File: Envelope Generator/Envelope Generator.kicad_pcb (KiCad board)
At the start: 2 copper layers, 91.3 x 104.5 mm, 71 parts, among them J101 Conn_02x05_Odd_Even, J201 AudioJack2_SwitchT, J301 AudioJack2_SwitchT, J302 AudioJack2_SwitchT, J303 AudioJack2_SwitchT, J304 AudioJack2_SwitchT, Q201 BC547, Q202 BC547, Q203 BC547, SW201 SW_SPST, SW202 SW_SPDT, U101 TL072, U102 TL072, U103 TL072, U104 TL072, U201 ICM7555xP

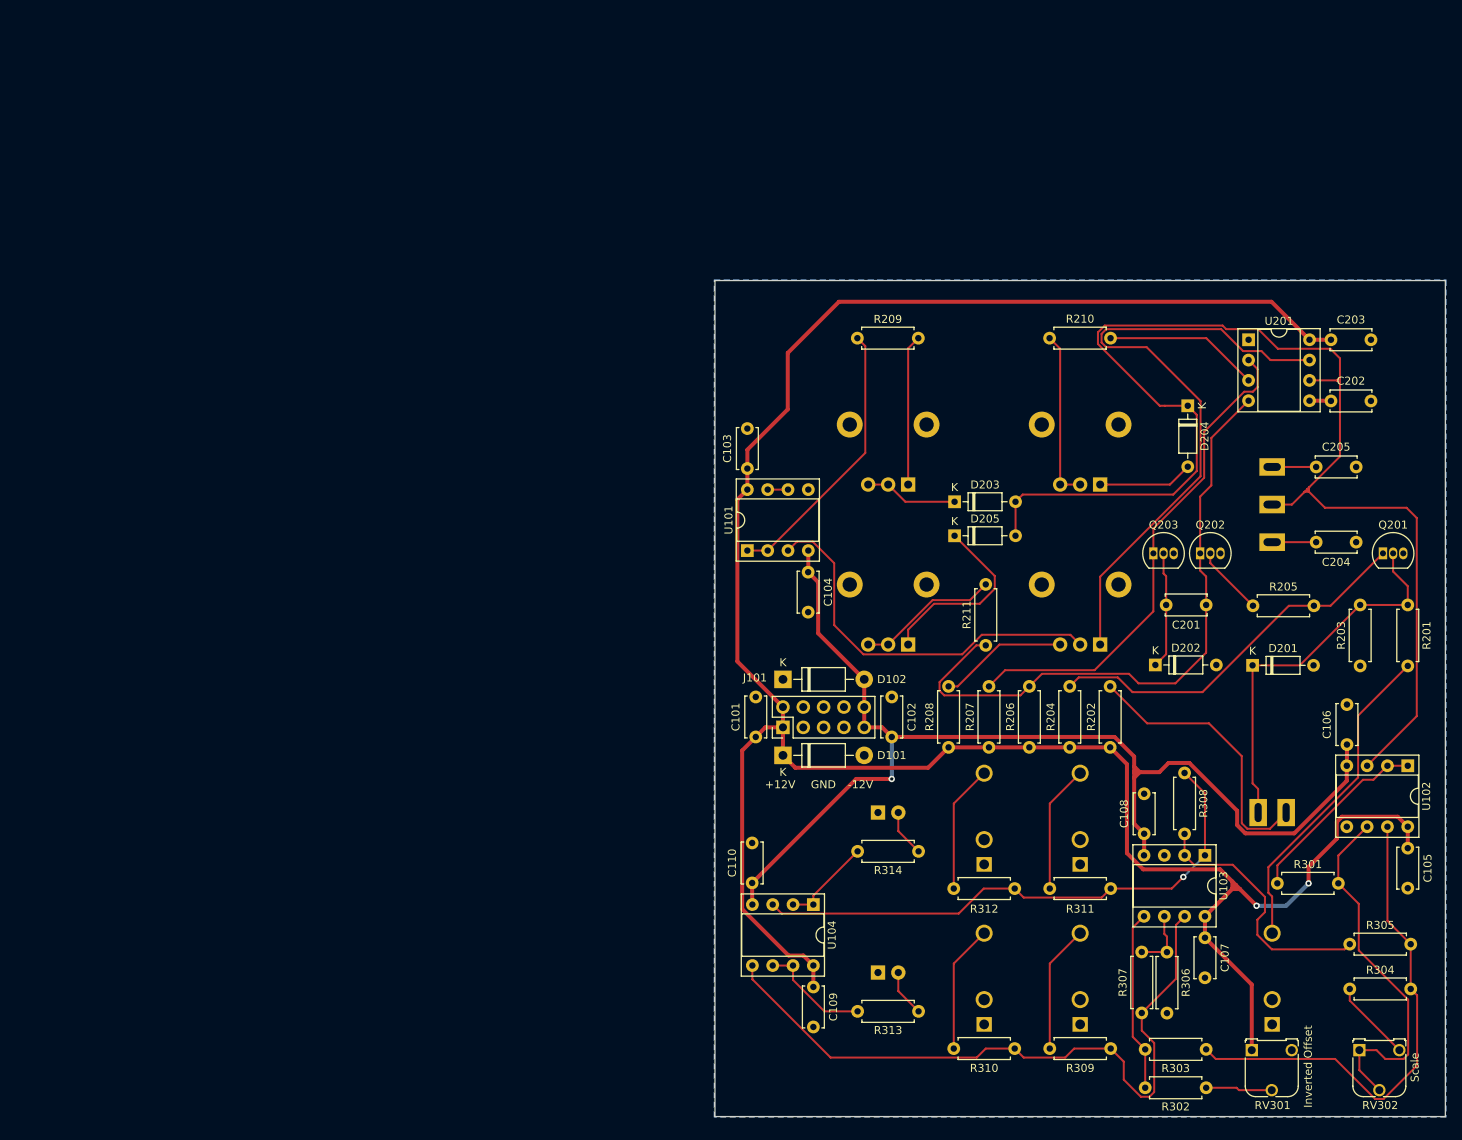
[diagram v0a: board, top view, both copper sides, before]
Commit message: New MIDI controller, new envelope generator
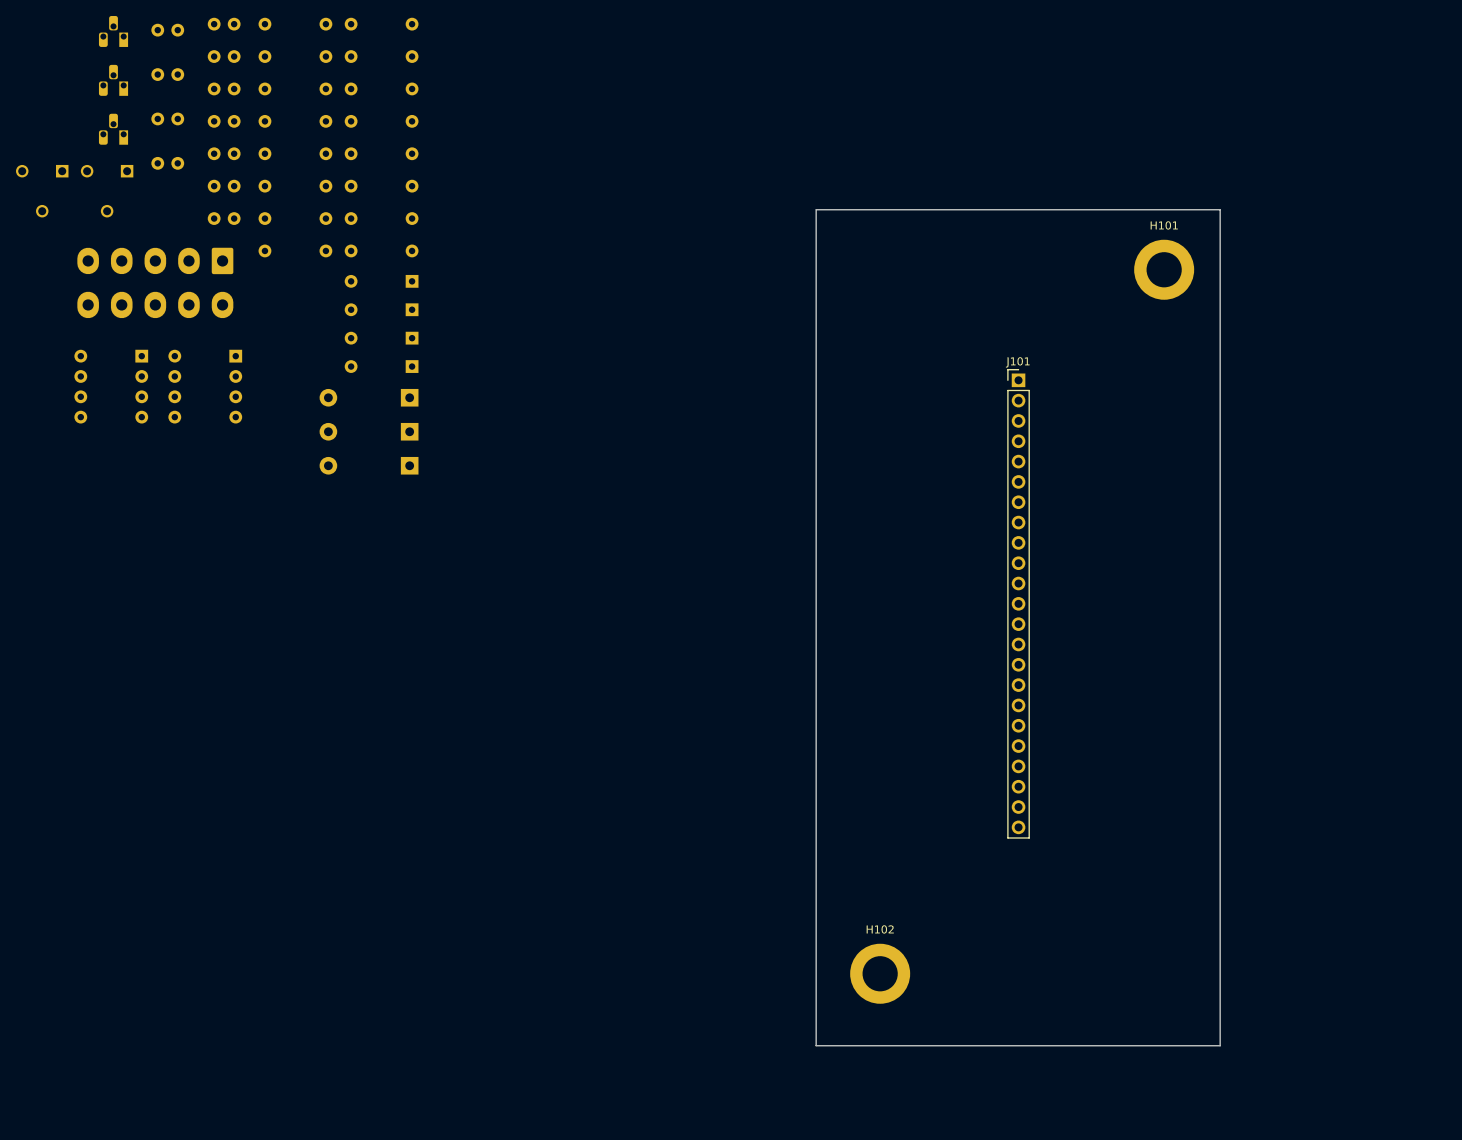
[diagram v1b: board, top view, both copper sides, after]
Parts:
- removed C101, C102, C203: 0.1u, Capacitor_THT:C_Disc_D5.0mm_W2.5mm_P5.00mm
- removed C103, C104, C105, C106, C107, C108, C109, C110, C201: 10n, Capacitor_THT:C_Disc_D5.0mm_W2.5mm_P5.00mm
- removed C202: 47n, Capacitor_THT:C_Disc_D5.0mm_W2.5mm_P5.00mm
- removed C204: 1u, Capacitor_THT:C_Disc_D5.0mm_W2.5mm_P5.00mm
- removed C205: 10u, Capacitor_THT:C_Disc_D5.0mm_W2.5mm_P5.00mm
- removed D101, D102: 1N5819, Diode_THT:D_DO-41_SOD81_P10.16mm_Horizontal
- removed D201, D202, D203, D204, D205: 1N4148, Diode_THT:D_DO-35_SOD27_P7.62mm_Horizontal
- removed D301, D302: LED, LED_THT:LED_D5.0mm
- removed J201, J301, J302, J303, J304: AudioJack2_SwitchT, Connector_Audio:Jack_3.5mm_QingPu_WQP-PJ398SM_Vertical_CircularHoles
- removed Q201, Q202, Q203: BC547, Package_TO_SOT_THT:TO-92_Inline
- removed R201: 56k, Resistor_THT:R_Axial_DIN0207_L6.3mm_D2.5mm_P7.62mm_Horizontal
- removed R202, R313, R314: 150k, Resistor_THT:R_Axial_DIN0207_L6.3mm_D2.5mm_P7.62mm_Horizontal
- removed R203: 560k, Resistor_THT:R_Axial_DIN0207_L6.3mm_D2.5mm_P7.62mm_Horizontal
- removed R204, R206, R207: 4.7k, Resistor_THT:R_Axial_DIN0207_L6.3mm_D2.5mm_P7.62mm_Horizontal
- removed R205: 10k, Resistor_THT:R_Axial_DIN0207_L6.3mm_D2.5mm_P7.62mm_Horizontal
- removed R208: 5.6k, Resistor_THT:R_Axial_DIN0207_L6.3mm_D2.5mm_P7.62mm_Horizontal
- removed R209, R309, R310, R311, R312: 1k, Resistor_THT:R_Axial_DIN0207_L6.3mm_D2.5mm_P7.62mm_Horizontal
- removed R210, R211: 100, Resistor_THT:R_Axial_DIN0207_L6.3mm_D2.5mm_P7.62mm_Horizontal
- removed R301: 68k, Resistor_THT:R_Axial_DIN0207_L6.3mm_D2.5mm_P7.62mm_Horizontal
- removed R302, R303, R306, R307: 75k, Resistor_THT:R_Axial_DIN0207_L6.3mm_D2.5mm_P7.62mm_Horizontal
- removed R304: 82k, Resistor_THT:R_Axial_DIN0207_L6.3mm_D2.5mm_P7.62mm_Horizontal
- removed R305, R308: 47k, Resistor_THT:R_Axial_DIN0207_L6.3mm_D2.5mm_P7.62mm_Horizontal
- removed RV201: 10k, Potentiometer_THT:Potentiometer_Alpha_RD901F-40-00D_Single_Vertical_CircularHoles
- removed RV202, RV203, RV204: 1M, Potentiometer_THT:Potentiometer_Alpha_RD901F-40-00D_Single_Vertical_CircularHoles
- removed RV301, RV302: 10k, Custom:Potentiometer_Runtron_RM-065_Vertical_Improved
- removed SW201: SW_SPST, Switch:PBS-105
- removed SW202: SW_SPDT, Switch:MTS-102_MTS-103_MTS-112_MTS-113_MTS-123
- removed U101, U102, U103, U104: TL072, Package_DIP:DIP-8_W7.62mm_Socket
- removed U201: ICM7555xP, Package_DIP:DIP-8_W7.62mm_Socket
- added C1: 10u, 0_Capacitor_THT:C_Disc_D5.5mm_W4.0mm_P2.50mm, B.Cu at (38.5, 22.8)
- added C10: 10p, 0_Capacitor_THT:C_Disc_D5.5mm_W2.5mm_P2.50mm, B.Cu at (45.5, 42.3)
- added C11: 4.7n, 0_Capacitor_THT:C_Disc_D5.5mm_W2.5mm_P2.50mm, B.Cu at (45.5, 46.4)
- added C2: 10u, 0_Capacitor_THT:C_Disc_D5.5mm_W4.0mm_P2.50mm, B.Cu at (38.5, 28.4)
- added C3: 10n, 0_Capacitor_THT:C_Disc_D5.5mm_W2.5mm_P2.50mm, B.Cu at (45.5, 22.1)
- added C4: 0.1u, 0_Capacitor_THT:C_Disc_D5.5mm_W2.5mm_P2.50mm, B.Cu at (45.5, 26.1)
- added C5: 0.1u, 0_Capacitor_THT:C_Disc_D5.5mm_W2.5mm_P2.50mm, B.Cu at (45.5, 30.1)
- added C6: 47n, 0_Capacitor_THT:C_Disc_D5.5mm_W2.5mm_P2.50mm, B.Cu at (45.5, 34.2)
- added C7: 0.1u, 0_Capacitor_THT:C_Disc_D5.5mm_W2.5mm_P2.50mm, B.Cu at (45.5, 38.2)
- added C8: 1u, 0_Capacitor_THT:C_Disc_D5.5mm_W4.0mm_P2.50mm, B.Cu at (38.5, 33.9)
- added C9: 10u, 0_Capacitor_THT:C_Disc_D5.5mm_W4.0mm_P2.50mm, B.Cu at (38.5, 39.5)
- added D1: 1N4148, Diode_THT:D_DO-35_SOD27_P7.62mm_Horizontal, B.Cu at (67.7, 54.2)
- added D2: 1N5819, Diode_THT:D_DO-41_SOD81_P10.16mm_Horizontal, B.Cu at (67.4, 68.8)
- added D3: 1N5819, Diode_THT:D_DO-41_SOD81_P10.16mm_Horizontal, B.Cu at (67.4, 73.0)
- added D4: 1N4148, Diode_THT:D_DO-35_SOD27_P7.62mm_Horizontal, B.Cu at (67.7, 57.8)
- added D5: 1N4148, Diode_THT:D_DO-35_SOD27_P7.62mm_Horizontal, B.Cu at (67.7, 61.3)
- added D6: 1N4148, Diode_THT:D_DO-35_SOD27_P7.62mm_Horizontal, B.Cu at (67.7, 64.8)
- added D7: 1N5819, Diode_THT:D_DO-41_SOD81_P10.16mm_Horizontal, B.Cu at (67.4, 77.2)
- added H101: MNT_STANDOFF, 0_MountingHole:MountingHole_Pitch7.5mm_Drill3.4mm, F.Cu at (161.8, 52.8)
- added H102: MNT_STANDOFF, 0_MountingHole:MountingHole_Pitch7.5mm_Drill3.4mm, F.Cu at (126.2, 140.8)
- added J2: Conn_02x05_Top_Bottom, Connector_Molex:Molex_Mini-Fit_Jr_5566-10A_2x05_P4.20mm_Vertical, B.Cu at (44.0, 51.6)
- added Q1: 2N3904, Package_TO_SOT_THT:TO-92_HandSolder, B.Cu at (31.7, 23.6)
- added Q2: 2N3904, Package_TO_SOT_THT:TO-92_HandSolder, B.Cu at (31.7, 29.7)
- added Q3: 2N3904, Package_TO_SOT_THT:TO-92_HandSolder, B.Cu at (31.7, 35.8)
- added R1: 100k, Resistor_THT:R_Axial_DIN0207_L6.3mm_D2.5mm_P7.62mm_Horizontal, B.Cu at (67.7, 22.1)
- added R10: 100, Resistor_THT:R_Axial_DIN0207_L6.3mm_D2.5mm_P7.62mm_Horizontal, B.Cu at (57.0, 26.1)
- added R11: 100, Resistor_THT:R_Axial_DIN0207_L6.3mm_D2.5mm_P7.62mm_Horizontal, B.Cu at (57.0, 30.1)
- added R12: 10k, Resistor_THT:R_Axial_DIN0207_L6.3mm_D2.5mm_P7.62mm_Horizontal, B.Cu at (57.0, 34.2)
- added R13: 47k, Resistor_THT:R_Axial_DIN0207_L6.3mm_D2.5mm_P7.62mm_Horizontal, B.Cu at (57.0, 38.2)
- added R14: 8.2k, Resistor_THT:R_Axial_DIN0207_L6.3mm_D2.5mm_P7.62mm_Horizontal, B.Cu at (57.0, 42.3)
- added R15: 1k, Resistor_THT:R_Axial_DIN0207_L6.3mm_D2.5mm_P7.62mm_Horizontal, B.Cu at (57.0, 46.4)
- added R16: 330k, Resistor_THT:R_Axial_DIN0207_L6.3mm_D2.5mm_P7.62mm_Horizontal, B.Cu at (57.0, 50.4)
- added R2: 100k, Resistor_THT:R_Axial_DIN0207_L6.3mm_D2.5mm_P7.62mm_Horizontal, B.Cu at (67.7, 26.1)
- added R3: 100k, Resistor_THT:R_Axial_DIN0207_L6.3mm_D2.5mm_P7.62mm_Horizontal, B.Cu at (67.7, 30.1)
- added R4: 4.7k, Resistor_THT:R_Axial_DIN0207_L6.3mm_D2.5mm_P7.62mm_Horizontal, B.Cu at (67.7, 34.2)
- added R5: 100k, Resistor_THT:R_Axial_DIN0207_L6.3mm_D2.5mm_P7.62mm_Horizontal, B.Cu at (67.7, 38.2)
- added R6: 4.7k, Resistor_THT:R_Axial_DIN0207_L6.3mm_D2.5mm_P7.62mm_Horizontal, B.Cu at (67.7, 42.3)
- added R7: 4.7k, Resistor_THT:R_Axial_DIN0207_L6.3mm_D2.5mm_P7.62mm_Horizontal, B.Cu at (67.7, 46.4)
- added R8: 5.6k, Resistor_THT:R_Axial_DIN0207_L6.3mm_D2.5mm_P7.62mm_Horizontal, B.Cu at (67.7, 50.4)
- added R9: 1k, Resistor_THT:R_Axial_DIN0207_L6.3mm_D2.5mm_P7.62mm_Horizontal, B.Cu at (57.0, 22.1)
- added RV5: 1k, Potentiometer_THT:Potentiometer_Runtron_RM-065_Vertical, B.Cu at (32.1, 40.4)
- added RV6: 10k, Potentiometer_THT:Potentiometer_Runtron_RM-065_Vertical, B.Cu at (24.0, 40.4)
- added U1: TL072, Package_DIP:DIP-8_W7.62mm_Socket, B.Cu at (45.7, 63.5)
- added U2: ICM7555xP, Package_DIP:DIP-8_W7.62mm_Socket, B.Cu at (34.0, 63.5)
- J101: value Conn_02x05_Odd_Even -> Conn_01x23; footprint Connector_PinHeader_2.54mm:PinHeader_2x05_P2.54mm_Vertical -> Connector_PinHeader_2.54mm:PinHeader_1x23_P2.54mm_Vertical
- moved J101 52.4 mm to (143.6, 66.6), turned to 0 degrees
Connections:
- J101 pad 1: +12V -> /SW_1
- J101 pad 10: -12V -> /SUS_3
- J101 pad 2: +12V -> /SW_2
- J101 pad 3: GND -> /SW_3
- J101 pad 4: GND -> /ATT_1
- J101 pad 5: GND -> /ATT_2
- J101 pad 6: GND -> /DEC_1
- J101 pad 7: GND -> /DEC_2
- J101 pad 8: GND -> /SUS_1
- J101 pad 9: -12V -> /SUS_2
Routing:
- net +12V: track 299.7 -> 0.00 mm, vias 2 -> 0
- net Net-(D203-Pad2): track 163.4 -> 0.00 mm
- net -12V: track 144.9 -> 0.00 mm, vias 1 -> 0
- net Net-(R307-Pad1): track 86.3 -> 0.00 mm
- net Net-(RV201-Pad1): track 80.0 -> 0.00 mm
- net Net-(C201-Pad1): track 79.8 -> 0.00 mm
- net Net-(R308-Pad1): track 69.8 -> 0.00 mm, vias 1 -> 0
- net Net-(Q203-Pad1): track 62.3 -> 0.00 mm
- net Net-(R303-Pad1): track 62.0 -> 0.00 mm
- net Net-(RV201-Pad2): track 48.9 -> 0.00 mm
- net Net-(D201-Pad1): track 48.4 -> 0.00 mm
- net Net-(Q201-Pad1): track 47.6 -> 0.00 mm
- net Net-(R301-Pad2): track 46.4 -> 0.00 mm
- net Net-(J201-PadT): track 40.8 -> 0.00 mm
- net Net-(R202-Pad2): track 35.1 -> 0.00 mm
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- removed copper zone on B.Cu, net GND
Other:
- board size 91.3 x 104.5 mm -> 50.5 x 104.5 mm
- board text removed: "+12V"
- board text removed: "-12V"
- board text removed: "GND"
- board text removed: "Inverted Offset"
- board text removed: "Scale"

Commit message: New VCLPF and Out
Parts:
- moved RV6 167.2 mm to (161.4, 135.8), turned to -90 degrees
- moved C4 158.7 mm to (149.3, 146.1), turned to 0 degrees
- moved RV5 156.5 mm to (161.4, 128.5), turned to -90 degrees
- moved C10 146.8 mm to (155.0, 140.1), turned to 90 degrees
- moved Q1 142.6 mm to (133.1, 123.9)
- moved C5 141.7 mm to (144.2, 131.9), turned to 0 degrees
- moved R14 141.2 mm to (158.2, 140.8), turned to 90 degrees
- moved R12 140.0 mm to (158.2, 130.9), turned to 90 degrees
- moved R15 138.0 mm to (155.0, 143.5), turned to 0 degrees
- moved R13 134.9 mm to (155.0, 130.9), turned to 90 degrees
- moved Q2 134.8 mm to (133.1, 118.6)
- moved C3 128.9 mm to (136.2, 113.7), turned to 90 degrees
- moved Q3 127.6 mm to (133.1, 113.3)
- moved U1 126.4 mm to (144.2, 142.7), turned to 0 degrees
- moved R3 121.0 mm to (139.4, 127.6)
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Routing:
- net +12V: track 0.00 -> 186.1 mm, vias 0 -> 1
- net -12V: track 0.00 -> 130.4 mm, vias 0 -> 2
- net /SW_2: track 0.00 -> 117.3 mm, vias 0 -> 2
- net Net-(U1A--): track 0.00 -> 76.1 mm, vias 0 -> 4
- net Chassis: track 0.00 -> 68.8 mm, vias 0 -> 3
- net Net-(Q2-C): track 0.00 -> 59.1 mm, vias 0 -> 1
- net /SUS_2: track 0.00 -> 58.3 mm, vias 0 -> 1
- net /OUT: track 0.00 -> 54.0 mm, vias 0 -> 2
- net Net-(D1-K): track 0.00 -> 45.0 mm
- net /REL_1: track 0.00 -> 29.5 mm
- net /SUS_1: track 0.00 -> 28.7 mm, vias 0 -> 1
- net Net-(U2-Q): track 0.00 -> 25.0 mm, vias 0 -> 2
- net Net-(Q3-C): track 0.00 -> 20.1 mm
- net Net-(R13-Pad2): track 0.00 -> 15.2 mm
- net /LED: track 0.00 -> 14.4 mm
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- added copper zone on B.Cu, net GND
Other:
- board text added: "Envelope V1 Matthew Taylor"
- board text added: "JLCJLCJLCJLC"
